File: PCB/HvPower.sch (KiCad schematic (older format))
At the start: 0 parts

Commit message: Add LMR62421 regulator and inductor to library, draw schematic for 12V supply, add HV-ENABLE pin to microcontroller
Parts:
- added C?: 10uF, Capacitors_SMD:C_0805_HandSoldering, symbol Device:C_Small
- added C?: 2.2nF, Capacitors_SMD:C_0603_HandSoldering, symbol Device:C_Small
- added C? (x3): 10uF, Capacitors_SMD:C_1206_HandSoldering, symbol Device:C_Small
- added D?: 550mV 2A, Diodes_SMD:D_SOD-123F, symbol Device:D_Schottky_Small_ALT
- added L?: 10uH, Parts:NRS6045T100MMGK, symbol Device:L_Core_Ferrite_Small
- added NT?: Net-Tie_2, symbol Device:Net-Tie_2
- added R?: 86.6k, Capacitors_SMD:C_0603_HandSoldering, symbol Device:R
- added R? (x2): 10k, Capacitors_SMD:C_0603_HandSoldering, symbol Device:R
- added U?: LMR62421, Parts:WSON6-3x3-PAD, symbol Parts:LMR62421
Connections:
- net labels added: +12V, +50V, +BATT, GNDA-12V, HV-ENABLE
- net labels removed: +48V
- wire segments 0 -> 42

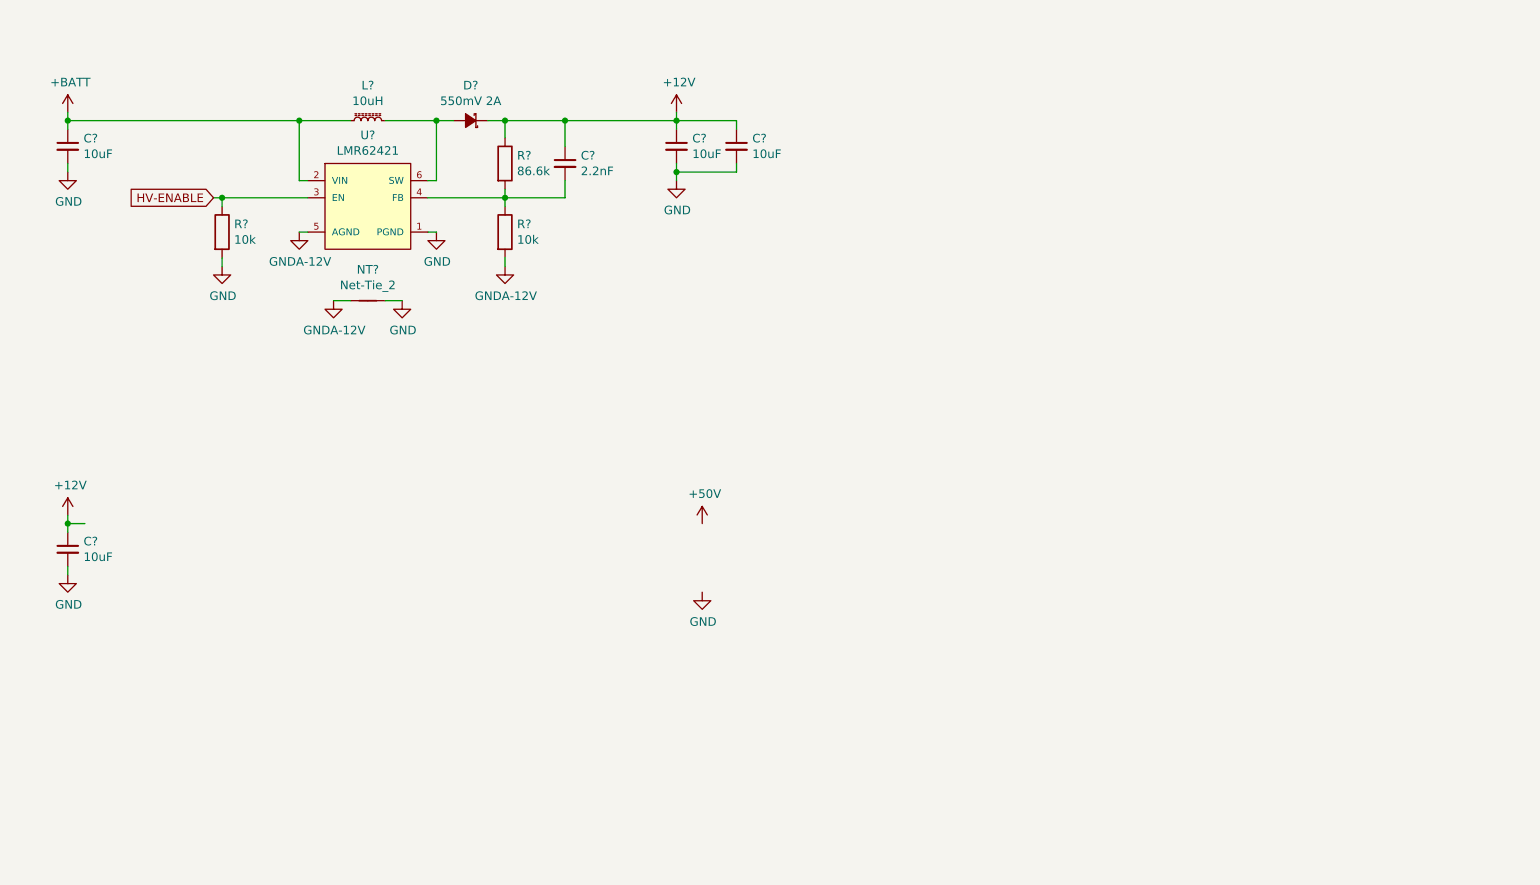
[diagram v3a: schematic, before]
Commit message: Add 50V regulator schematic, change 12V diode to be the same as 50V diode
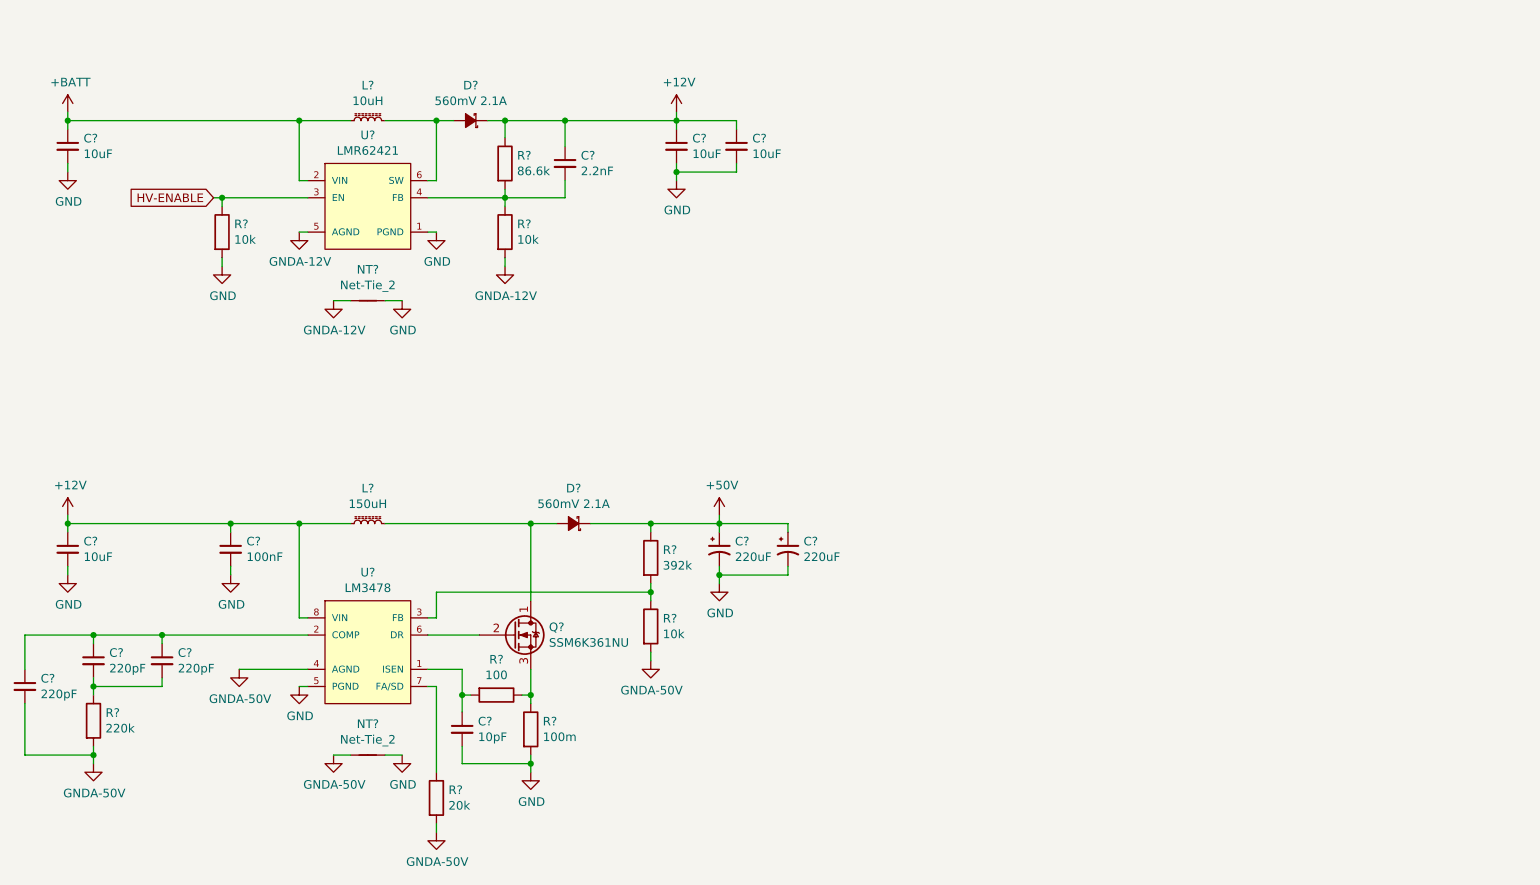
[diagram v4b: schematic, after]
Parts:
- removed D?: 550mV 2A, Diodes_SMD:D_SOD-123F, symbol Device:D_Schottky_Small_ALT
- added C?: 10pF, Capacitors_SMD:C_0603_HandSoldering, symbol Device:C_Small
- added C? (x2): 220uF, Capacitors_THT:CP_Radial_D10.0mm_P5.00mm, symbol Device:CP1_Small
- added C? (x3): 220pF, Capacitors_SMD:C_0603_HandSoldering, symbol Device:C_Small
- added C?: 100nF, Capacitors_SMD:C_0603_HandSoldering, symbol Device:C_Small
- added D? (x2): 560mV 2.1A, Diodes_SMD:D_SOD-123F, symbol Device:D_Schottky_Small_ALT
- added L?: 150uH, Parts:SRU1048-151Y, symbol Device:L_Core_Ferrite_Small
- added NT?: Net-Tie_2, symbol Device:Net-Tie_2
- added Q?: SSM6K361NU, Parts:UDFN6-FET-PAD, symbol Device:Q_NMOS_DGS
- added R?: 10k, Capacitors_SMD:C_0603_HandSoldering, symbol Device:R
- added R?: 392k, Capacitors_SMD:C_0603_HandSoldering, symbol Device:R
- added R?: 100m, Capacitors_SMD:C_0603_HandSoldering, symbol Device:R
- added R?: 100, Capacitors_SMD:C_0603_HandSoldering, symbol Device:R
- added R?: 20k, Capacitors_SMD:C_0603_HandSoldering, symbol Device:R
- added R?: 220k, Capacitors_SMD:C_0603_HandSoldering, symbol Device:R
- added U?: LM3478, Parts:SSOP8, symbol Parts:LM3478
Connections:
- net +12V: now also C?.1, D?.1 (K), L?.1, U?.8 (VIN)
- net +50V: now also C?.1, C?.1, D?.1 (K), R?.1
- net GND: now also C?.2, C?.2, C?.2, C?.2, NT?.2, R?.2, U?.5 (PGND)
- net at L?.2, U?.6 (SW): now also D?.2 (A)
- new net: C?.1, R?.2, U?.1 (ISEN)
- new net: C?.1, C?.1, C?.1, U?.2 (COMP)
- new net: R?.1, R?.2, U?.3 (FB)
- new net: Q?.2 (G), U?.6 (DR)
- new net: R?.1, U?.7 (FA/SD)
- new net: D?.2 (A), L?.2, Q?.1 (D)
- new net: Q?.3 (S), R?.1, R?.1
- new net: C?.2, C?.2, R?.1
- new net GNDA-50V: C?.2, NT?.1, R?.2, R?.2, R?.2, U?.4 (AGND)

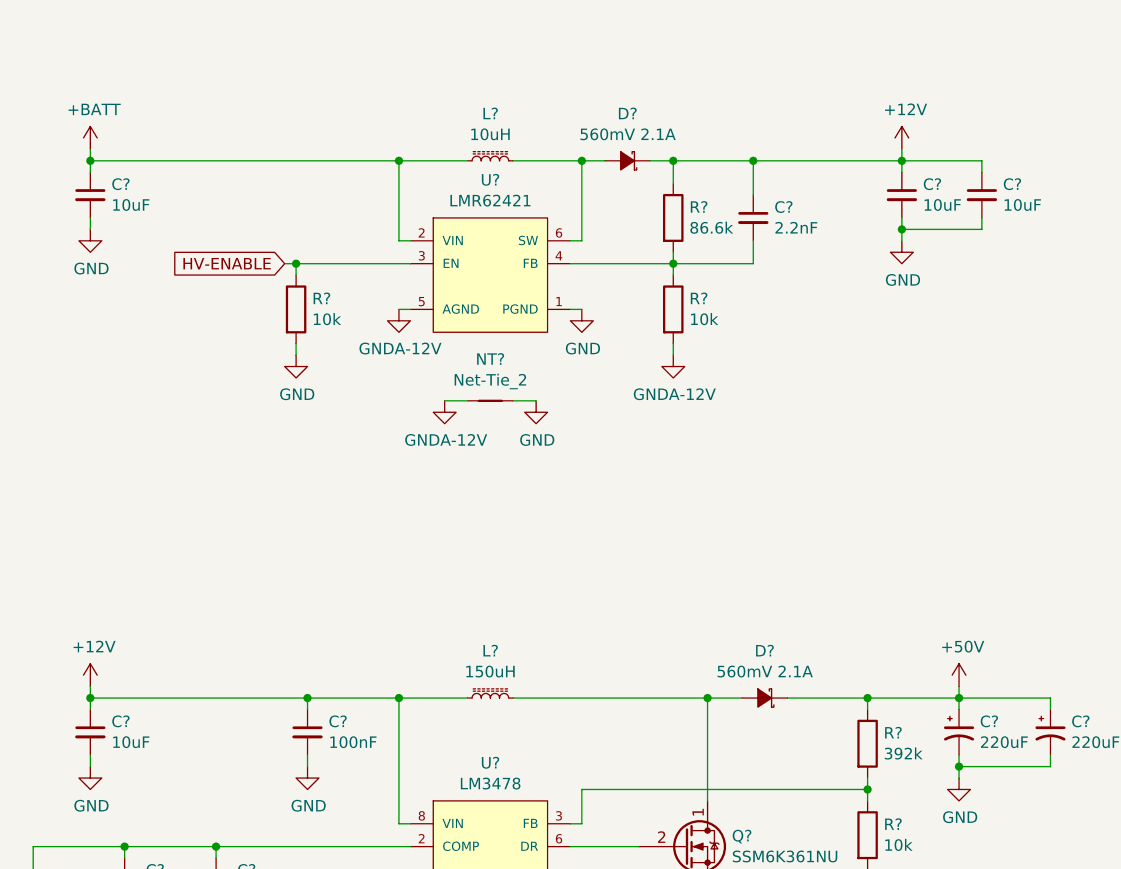
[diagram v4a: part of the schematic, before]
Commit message: Touchup footprints, add soldered jumpers to HV power supplies
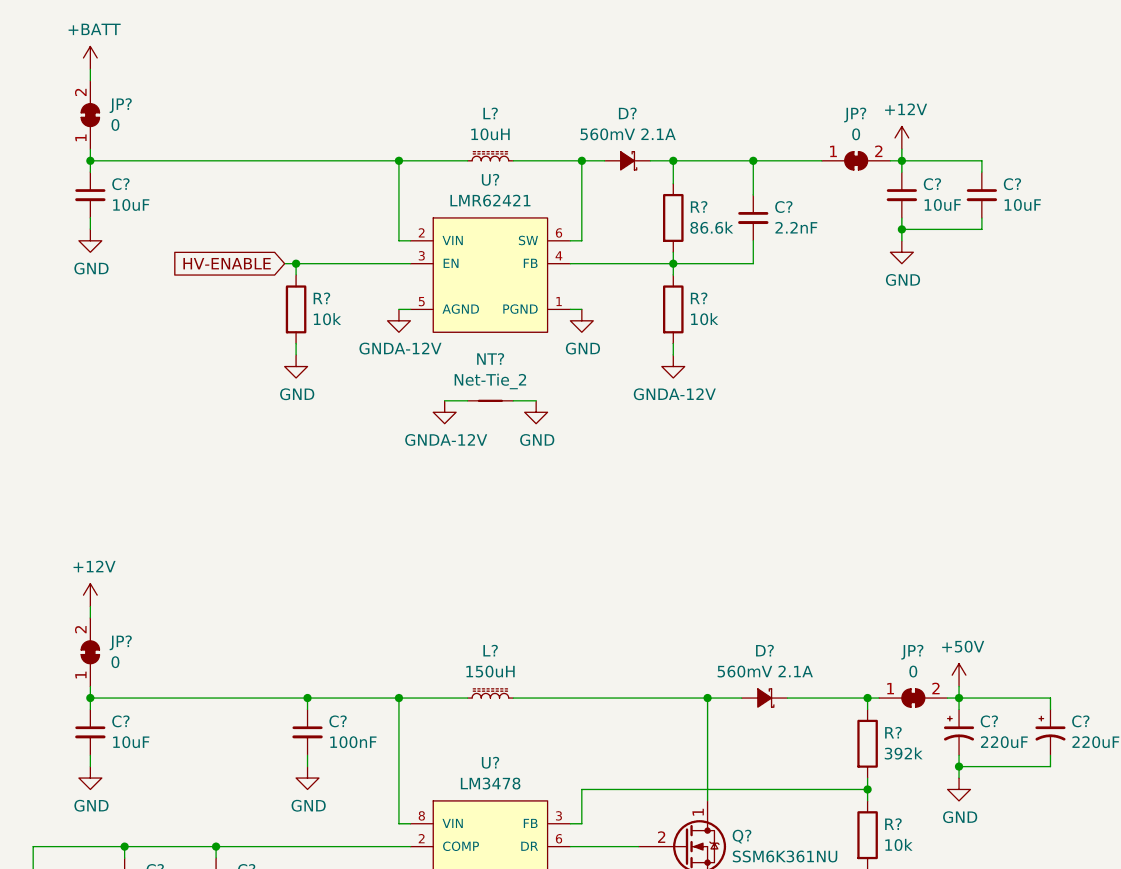
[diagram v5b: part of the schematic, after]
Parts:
- added JP? (x4): 0, Parts:SolderJumper_0603, symbol Jumper:SolderJumper_2_Bridged
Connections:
- net +12V: now also JP?.2 (B), JP?.2 (B); no longer C?.1, C?.1, C?.1, D?.1 (K), L?.1, R?.1, U?.8 (VIN)
- net +50V: now also JP?.2 (B); no longer D?.1 (K), R?.1
- net +BATT: now also JP?.2 (B); no longer C?.1, L?.1, U?.2 (VIN)
- new net: C?.1, JP?.1 (A), L?.1, U?.2 (VIN)
- new net: C?.1, D?.1 (K), JP?.1 (A), R?.1
- new net: C?.1, C?.1, JP?.1 (A), L?.1, U?.8 (VIN)
- new net: D?.1 (K), JP?.1 (A), R?.1
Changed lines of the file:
@@
 L power:+BATT #PWR?
 U 1 1 5DDF98F8
-P 2150 2350
-F 0 "#PWR?" H 2150 2200 50  0001 C CNN
-F 1 "+BATT" H 2165 2523 50  0000 C CNN
-F 2 "" H 2150 2350 50  0001 C CNN
-F 3 "" H 2150 2350 50  0001 C CNN
-	1    2150 2350
+P 2150 2000
+F 0 "#PWR?" H 2150 1850 50  0001 C CNN
+F 1 "+BATT" H 2165 2173 50  0000 C CNN
+F 2 "" H 2150 2000 50  0001 C CNN
+F 3 "" H 2150 2000 50  0001 C CNN
+	1    2150 2000
 	1    0    0    -1
 $EndComp
@@
 	5050 2400 4700 2400
 Wire Wire Line
-	5050 2400 5700 2400
+	5050 2400 5350 2400
 $Comp
 L Device:L_Core_Ferrite_Small L?
@@
 	4700 2850 4250 2850
 Wire Wire Line
-	2150 2350 2150 2400
-Connection ~ 2150 2400
-Wire Wire Line
 	2150 2400 2150 2450
 $Comp
@@
 L power:+12V #PWR?
 U 1 1 5DE44608
-P 2150 4700
-F 0 "#PWR?" H 2150 4550 50  0001 C CNN
-F 1 "+12V" H 2165 4873 50  0000 C CNN
-F 2 "" H 2150 4700 50  0001 C CNN
-F 3 "" H 2150 4700 50  0001 C CNN
-	1    2150 4700
+P 2150 4350
+F 0 "#PWR?" H 2150 4200 50  0001 C CNN
+F 1 "+12V" H 2165 4523 50  0000 C CNN
+F 2 "" H 2150 4350 50  0001 C CNN
+F 3 "" H 2150 4350 50  0001 C CNN
+	1    2150 4350
 	1    0    0    -1
 $EndComp
@@
 	2150 5050 2150 5000
 Wire Wire Line
-	2150 4700 2150 4750
+	2150 4350 2150 4400
 Connection ~ 2150 4750
 Wire Wire Line
@@
 Wire Wire Line
 	3050 2850 3550 2850
-Wire Wire Line
-	2150 2400 3500 2400
 Connection ~ 3500 2400
 $Comp
@@
 	3500 5700 3550 5700
 Wire Wire Line
-	2150 4750 3100 4750
-Wire Wire Line
 	3500 4750 3500 5300
 Wire Wire Line
@@
 $EndComp
 Wire Wire Line
-	5550 4750 5950 4750
+	5550 4750 5600 4750
 Wire Wire Line
 	5950 4750 5950 4700
@@
 Wire Wire Line
 	3100 4750 3500 4750
+$Comp
+L Jumper:SolderJumper_2_Bridged JP?
+U 1 1 5DE5A1EB
+P 2150 2200
+F 0 "JP?" V 2196 2112 50  0000 R CNN
+F 1 "0" V 2105 2112 50  0000 R CNN
+F 2 "Parts:SolderJumper_0603" H 2150 2200 50  0001 C CNN
+F 3 "" H 2150 2200 50  0001 C CNN
+	1    2150 2200
+	0    -1   -1   0
+$EndComp
+Wire Wire Line
+	2150 2400 3500 2400
+Wire Wire Line
+	2150 2400 2150 2350
+Connection ~ 2150 2400
+Wire Wire Line
+	2150 2050 2150 2000
+Wire Wire Line
+	2150 4750 3100 4750
+$Comp
+L Jumper:SolderJumper_2_Bridged JP?
+U 1 1 5DE833A1
+P 2150 4550
+F 0 "JP?" V 2196 4462 50  0000 R CNN
+F 1 "0" V 2105 4462 50  0000 R CNN
+F 2 "Parts:SolderJumper_0603" H 2150 4550 50  0001 C CNN
+F 3 "" H 2150 4550 50  0001 C CNN
+	1    2150 4550
+	0    -1   -1   0
+$EndComp
+Wire Wire Line
+	2150 4700 2150 4750
+$Comp
+L Jumper:SolderJumper_2_Bridged JP?
+U 1 1 5DE88746
+P 5500 2400
+F 0 "JP?" H 5500 2605 50  0000 C CNN
+F 1 "0" H 5500 2514 50  0000 C CNN
+F 2 "Parts:SolderJumper_0603" H 5500 2400 50  0001 C CNN
+F 3 "" H 5500 2400 50  0001 C CNN
+	1    5500 2400
+	1    0    0    -1
+$EndComp
+Wire Wire Line
+	5650 2400 5700 2400
+$Comp
+L Jumper:SolderJumper_2_Bridged JP?
+U 1 1 5DE89AF1
+P 5750 4750
+F 0 "JP?" H 5750 4955 50  0000 C CNN
+F 1 "0" H 5750 4864 50  0000 C CNN
+F 2 "Parts:SolderJumper_0603" H 5750 4750 50  0001 C CNN
+F 3 "" H 5750 4750 50  0001 C CNN
+	1    5750 4750
+	1    0    0    -1
+$EndComp
+Wire Wire Line
+	5900 4750 5950 4750
 $EndSCHEMATC

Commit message: Added soldered jumpers to LV power schematic
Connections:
- net +12V: now also JP?.1 (A); no longer JP?.2 (B)
- net +BATT: now also JP?.1 (A); no longer JP?.2 (B)
- net at C?.1, L?.1, U?.2 (VIN): now also JP?.2 (B); no longer JP?.1 (A)
- net at C?.1, C?.1, L?.1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: now also JP?.2 (B); no longer JP?.1 (A)
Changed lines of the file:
@@
 U 1 1 5DE5A1EB
 P 2150 2200
-F 0 "JP?" V 2196 2112 50  0000 R CNN
-F 1 "0" V 2105 2112 50  0000 R CNN
+F 0 "JP?" V 2104 2268 50  0000 L CNN
+F 1 "0" V 2195 2268 50  0000 L CNN
 F 2 "Parts:SolderJumper_0603" H 2150 2200 50  0001 C CNN
 F 3 "" H 2150 2200 50  0001 C CNN
 	1    2150 2200
-	0    -1   -1   0
+	0    1    1    0
 $EndComp
 Wire Wire Line
@@
 U 1 1 5DE833A1
 P 2150 4550
-F 0 "JP?" V 2196 4462 50  0000 R CNN
-F 1 "0" V 2105 4462 50  0000 R CNN
+F 0 "JP?" V 2104 4618 50  0000 L CNN
+F 1 "0" V 2195 4618 50  0000 L CNN
 F 2 "Parts:SolderJumper_0603" H 2150 4550 50  0001 C CNN
 F 3 "" H 2150 4550 50  0001 C CNN
 	1    2150 4550
-	0    -1   -1   0
+	0    1    1    0
 $EndComp
 Wire Wire Line
